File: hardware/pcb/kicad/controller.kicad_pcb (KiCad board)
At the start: 6 copper layers, 160 x 100 mm, 0 parts

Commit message: feat(hardware): complete reproducible engineering release artifacts
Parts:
- added F1: FUSE_10A, , F.Cu at (48.0, 35.0)
- added H1: M3_NPTH, , F.Cu at (24.0, 24.0)
- added H2: M3_NPTH, , F.Cu at (176.0, 24.0)
- added H3: M3_NPTH, , F.Cu at (176.0, 116.0)
- added H4: M3_NPTH, , F.Cu at (24.0, 116.0)
- added J1: 48V_INPUT_10A, , F.Cu at (30.0, 35.0)
- added J10: ESTOP_RED_KEYED, , F.Cu at (150.0, 110.0)
- added J2: 12V_OUTPUT_16A, , F.Cu at (72.0, 82.0)
- added J3: JETSON_5V_12A, , F.Cu at (148.0, 42.0)
- added J5: CAN_A, , F.Cu at (150.0, 96.0)
- added J6: CAN_B, , F.Cu at (168.0, 96.0)
- added U1: LM5069_HOTSWAP, , F.Cu at (68.0, 35.0)
- added U2: DCM3623_48V_12V_240W, , F.Cu at (88.0, 35.0)
- added U3: BUCK_12V_5V_10A, , F.Cu at (112.0, 42.0)
- added U4: BUCK_12V_3V3_5A, , F.Cu at (112.0, 64.0)
- added U5: CH32V307_CARRIER, , F.Cu at (145.0, 64.0)
- added U6: ISO1042DW, , F.Cu at (112.0, 96.0)
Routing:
- net GND: track 0.00 -> 704.0 mm
- net 12V_ISO: track 0.00 -> 220.0 mm
- net 3V3_LOGIC: track 0.00 -> 210.0 mm
- net VBAT_FUSED: track 0.00 -> 150.5 mm
- net GND_PWR: track 0.00 -> 83.5 mm
- net CANL: track 0.00 -> 70.0 mm
- net CANH: track 0.00 -> 70.0 mm
- net 5V_JETSON: track 0.00 -> 53.0 mm
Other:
- board text added: "8 mm ISOLATION BARRIER"
- board text added: "LOGIC / INTERFACES"
- board text added: "POWER DOMAIN"
- board text added: "WORKBENCH-1 CONTROLLER REV A"
- board text removed: "8 mm ISOLATION BARRIER - NO COPPER"
- board text removed: "WORKBENCH-1 CONTROLLER - NOT FOR FABRICATION"

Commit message: feat(hardware): close EVT interface and isolation review
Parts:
- added J4: JETSON_MCU_BACKPLANE, , F.Cu at (145.0, 140.0)
- added U7: 3V3_5V_ISOLATED_DC_DC, , F.Cu at (165.0, 77.0)
- J3: value JETSON_5V_12A -> JETSON_DEVKIT_12V_5A
- U3: value BUCK_12V_5V_10A -> JETSON_12V_EFUSE_5A
- moved J10 85.4 mm to (70.0, 140.0)
- moved U5 46.0 mm to (145.0, 110.0)
- moved J5 41.3 mm to (145.0, 55.0)
- moved J6 41.1 mm to (165.0, 55.0)
- moved U6 38.1 mm to (145.0, 77.0)
- moved J2 34.0 mm to (106.0, 82.0)
- moved H3 30.0 mm to (176.0, 146.0)
- moved H4 30.0 mm to (24.0, 146.0)
- moved J3 23.0 mm to (125.0, 42.0)
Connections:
- net 5V_JETSON renamed JETSON_12V
- J5 pad 3: GND -> GND_CAN_ISO
- J6 pad 3: GND -> GND_CAN_ISO
- U5 pad 2: 3V3_LOGIC -> GND
- U5 pad 4: 3V3_LOGIC -> GND
- U5 pad 5: GND -> SPI_SCLK
- U5 pad 6: GND -> SPI_MOSI
- U5 pad 7: GND -> SPI_MISO
- U5 pad 8: GND -> MOTOR_ENABLE
- U6 pad 1: 3V3_LOGIC -> 5V_CAN_ISO
- U6 pad 2: GND -> GND_CAN_ISO
- U6 pad 3: (no net) -> CANH
- U6 pad 4: (no net) -> CANL
- U6 pad 5: CANH -> 3V3_LOGIC
- U6 pad 6: CANL -> GND
- U6 pad 7: GND -> CAN_TX
- U6 pad 8: 3V3_LOGIC -> CAN_RX
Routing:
- net GND: track 704.0 -> 930.8 mm
- net 12V_ISO: track 220.0 -> 158.5 mm
- net GND_CAN_ISO: track 0.00 -> 59.0 mm
- net CAN_TX: track 0.00 -> 47.6 mm
- net CAN_RX: track 0.00 -> 47.4 mm
- net UART_TX: track 0.00 -> 30.1 mm
- net UART_RX: track 0.00 -> 30.1 mm
- net SPI_SCLK: track 0.00 -> 30.1 mm
- net SPI_MOSI: track 0.00 -> 30.1 mm
- net SPI_MISO: track 0.00 -> 30.1 mm
- net MOTOR_ENABLE: track 0.00 -> 30.1 mm
- net MOTOR_CS5: track 0.00 -> 30.1 mm
- net MOTOR_CS4: track 0.00 -> 30.1 mm
- net MOTOR_CS3: track 0.00 -> 30.1 mm
- net MOTOR_CS2: track 0.00 -> 30.1 mm
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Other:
- board size 160 x 100 mm -> 160 x 130 mm
- board text added: "CAN ISOLATION"

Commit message: feat(hardware): harden safety and order release gates
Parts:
- added J11: SAFETY_GATE_OUTPUT, , F.Cu at (135.0, 92.0)
- added U8: DUAL_CHANNEL_SAFETY_GATE_CARRIER, , F.Cu at (110.0, 125.0)
- J10: value ESTOP_RED_KEYED -> ESTOP_RED_KEYED_DUAL_CHANNEL
- moved J10 38.0 mm to (108.0, 140.0)
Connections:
- net MOTOR_ENABLE renamed MOTOR_ENABLE_REQ
- J10 pad 1: (no net) -> ESTOP_CH_A_OUT
- J10 pad 2: (no net) -> ESTOP_CH_A_RETURN
- J10 pad 3: (no net) -> ESTOP_CH_B_OUT
- J10 pad 4: (no net) -> ESTOP_CH_B_RETURN
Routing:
- net ESTOP_SENSE: track 30.1 -> 170.3 mm, vias 0 -> 2
- net GND: track 930.8 -> 1023.4 mm, vias 0 -> 3
- net MOTOR_ENABLE_REQ: track 30.1 -> 93.5 mm, vias 0 -> 1
- net MOTOR_ENABLE_SAFE: track 0.00 -> 60.0 mm
- net 12V_ISO: track 158.5 -> 204.0 mm, vias 0 -> 1
- net 3V3_LOGIC: track 190.3 -> 207.9 mm, vias 0 -> 1
- net ESTOP_CH_A_OUT: track 0.00 -> 16.0 mm
- net ESTOP_CH_A_RETURN: track 0.00 -> 15.7 mm
- net ESTOP_CH_B_OUT: track 0.00 -> 15.4 mm
- net ESTOP_CH_B_RETURN: track 0.00 -> 15.2 mm

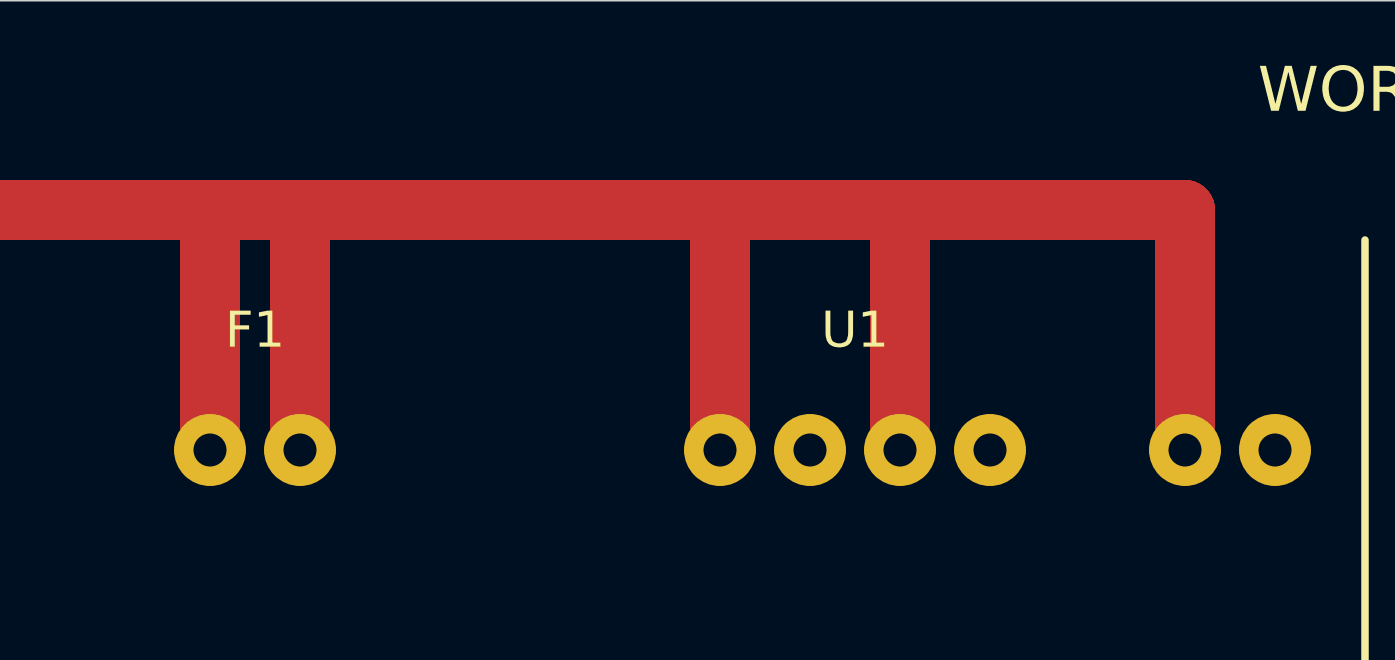
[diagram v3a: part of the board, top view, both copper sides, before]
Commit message: feat(hardware): audit protected input connectivity
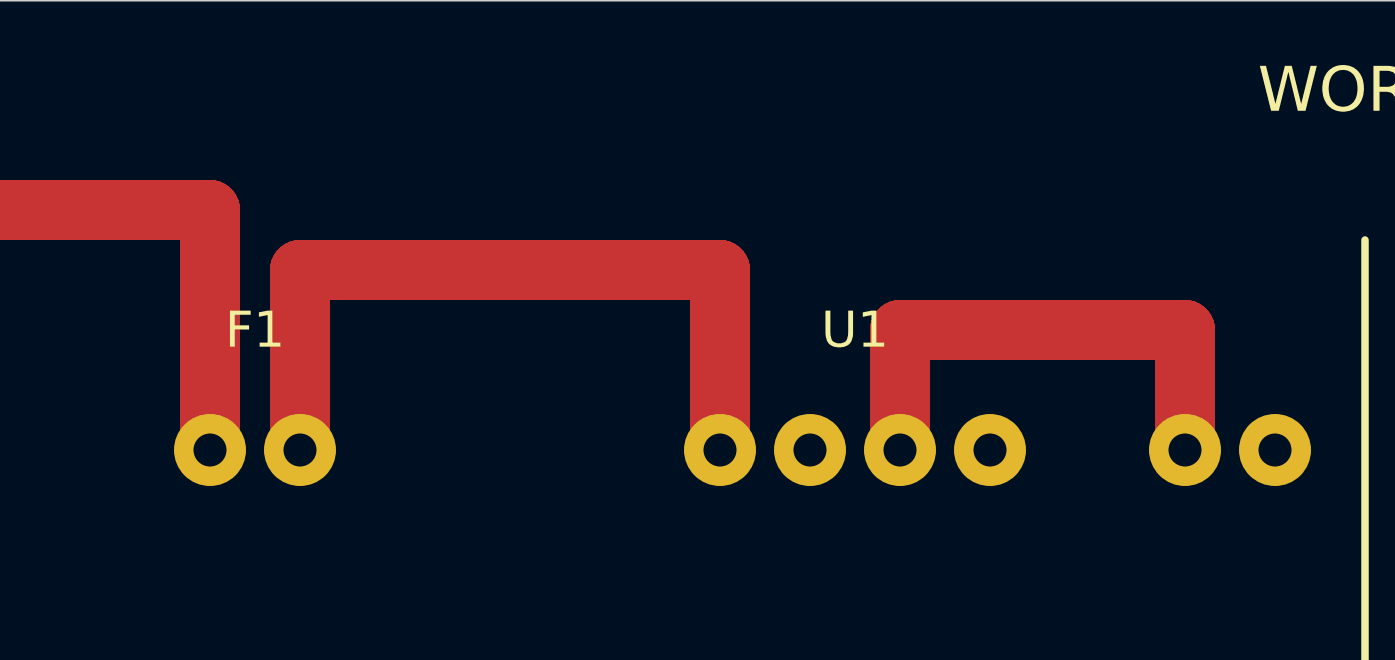
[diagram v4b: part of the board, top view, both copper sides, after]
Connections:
- F1 pad 1: VBAT_FUSED -> VBAT_RAW
- J1 pad 1: VBAT_FUSED -> VBAT_RAW
- J1 pad 2: VBAT_FUSED -> VBAT_RAW
- U1 pad 3: VBAT_FUSED -> VBAT_PROTECTED
- U2 pad 1: VBAT_FUSED -> VBAT_PROTECTED
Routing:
- net VBAT_FUSED: track 149.5 -> 26.0 mm
- net VBAT_RAW: track 0.00 -> 53.0 mm
- net VBAT_PROTECTED: track 0.00 -> 17.5 mm

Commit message: feat(hardware): add measured testpoint coverage
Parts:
- added TP1: VBAT_PROTECTED, , F.Cu at (69.5, 42.0)
- added TP2: 12V_ISO, , F.Cu at (101.5, 88.0)
- added TP3: JETSON_12V, , F.Cu at (120.5, 48.0)
- added TP4: 3V3_LOGIC, , F.Cu at (113.5, 70.0)
- added TP5: GND, , F.Cu at (116.5, 70.0)
- added TP6: CANH, , F.Cu at (140.5, 48.0)
- added TP7: CANL, , F.Cu at (143.5, 48.0)
- added TP8: MCU_RESET, , F.Cu at (168.4, 103.0)
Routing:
- net VBAT_PROTECTED: track 17.5 -> 24.5 mm
- net MCU_RESET: track 30.1 -> 37.1 mm
- net CANL: track 44.0 -> 51.0 mm
- net CANH: track 44.0 -> 51.0 mm
- net JETSON_12V: track 30.0 -> 36.0 mm
- net GND: track 1023.4 -> 1029.4 mm
- net 3V3_LOGIC: track 207.9 -> 213.9 mm
- net 12V_ISO: track 204.0 -> 210.0 mm

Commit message: feat(hardware): complete service robot engineering baseline
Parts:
- added C1: 1uF 100V, C_1210_3225Metric, F.Cu at (31.0, 36.0)
- added C10: 100nF, C_0603_1608Metric, F.Cu at (95.5, 102.5)
- added C11: 100nF, C_0603_1608Metric, F.Cu at (95.5, 105.7)
- added C12: 100nF, C_0603_1608Metric, F.Cu at (95.5, 108.9)
- added C13: 100nF, C_0603_1608Metric, F.Cu at (100.8, 113.0)
- added C14: 100nF, C_0603_1608Metric, F.Cu at (111.8, 113.0)
- added C15: 100nF, C_0603_1608Metric, F.Cu at (116.0, 97.2)
- added C16: 100nF, C_0603_1608Metric, F.Cu at (100.2, 93.0)
- added C17: 4.7uF, C_0805_2012Metric, F.Cu at (108.0, 91.5)
- added C18: 100nF, C_0603_1608Metric, F.Cu at (112.0, 18.0)
- added C19: 100nF, C_0603_1608Metric, F.Cu at (122.0, 111.0)
- added C2: 10uF 100V, C_2220_5750Metric, F.Cu at (42.0, 31.5)
- added C20: 1uF 10V, C_0603_1608Metric, F.Cu at (110.0, 46.8)
- added C3: 470uF 25V, CP_Radial_D12.5mm_P5.00mm, F.Cu at (93.0, 27.0)
- added C4: 1uF 25V, C_0805_2012Metric, F.Cu at (110.5, 6.50)
- added C40: 100nF, C_0603_1608Metric, F.Cu at (127.8, 36.2)
- added C41: 100nF, C_0603_1608Metric, F.Cu at (142.2, 36.2)
- added C42: 4.7uF, C_0805_2012Metric, F.Cu at (133.2, 18.0)
- added C43: 4.7uF, C_0805_2012Metric, F.Cu at (144.7, 18.0)
- added C44: 100nF, C_0603_1608Metric, F.Cu at (142.2, 42.5)
- added C5: 220uF 25V, CP_Radial_D10.0mm_P5.00mm, F.Cu at (119.0, 20.5)
- added C6: 22uF 25V, C_1210_3225Metric, F.Cu at (92.0, 43.5)
- added C7: 47uF 10V, C_1210_3225Metric, F.Cu at (87.5, 56.5)
- added C8: 47uF 10V, C_1210_3225Metric, F.Cu at (93.0, 56.5)
- added C9: 100nF, C_0603_1608Metric, F.Cu at (95.5, 99.3)
- added CG1: 4.7nF 100V, C_0603_1608Metric, F.Cu at (25.5, 26.5)
- added CSS4: 22nF, C_0603_1608Metric, F.Cu at (106.0, 46.8)
- added CY1: 18pF, C_0603_1608Metric, F.Cu at (88.5, 102.5)
- added CY2: 18pF, C_0603_1608Metric, F.Cu at (92.0, 106.5)
- added D1: SMCJ58A, D_SMC, F.Cu at (32.0, 10.5)
- added D2: CAN FD TVS, CAN_TVS, F.Cu at (150.0, 53.0)
- added D3: FLYBACK, D_SOD-123, F.Cu at (20.0, 82.5)
- added D4: FLYBACK, D_SOD-123, F.Cu at (20.0, 103.5)
- added F2: PTC 0.25A, Fuse_1206_3216Metric, F.Cu at (62.3, 86.2)
- added J12: DUAL MANUAL RESET, MicroFit_2x2, F.Cu at (71.0, 107.0)
- added J13: WCH DEBUG, PinHeader_1x04_P2.54mm_Vertical, F.Cu at (134.0, 115.5)
- added JP1: CAN TERM, PinHeader_1x02_P2.54mm_Vertical, F.Cu at (148.0, 84.0)
- added K1: FORCE-GUIDED 12V A, Panasonic_SFM4, F.Cu at (29.0, 93.0)
- added K2: FORCE-GUIDED 12V B, Panasonic_SFM4, F.Cu at (29.0, 114.0)
- added L1: 100R@100MHz, ACT45B, F.Cu at (144.0, 48.0)
- added Q1: 150V N-MOS, Infineon_PG-TDSON-8_6.15x5.15mm, F.Cu at (22.0, 21.0)
- added Q2: 150V N-MOS, Infineon_PG-TDSON-8_6.15x5.15mm, F.Cu at (30.0, 21.0)
- added R30: 33R, R_0603_1608Metric, F.Cu at (100.0, 118.0)
- added R31: 33R, R_0603_1608Metric, F.Cu at (104.0, 118.0)
- added R32: 33R, R_0603_1608Metric, F.Cu at (108.0, 118.0)
- added R33: 33R, R_0603_1608Metric, F.Cu at (112.0, 118.0)
- added R34: 33R, R_0603_1608Metric, F.Cu at (116.0, 118.0)
- added R35: 33R, R_0603_1608Metric, F.Cu at (120.0, 118.0)
- added R36: 33R, R_0603_1608Metric, F.Cu at (124.0, 118.0)
- added R37: 33R, R_0603_1608Metric, F.Cu at (100.0, 123.0)
- added R38: 33R, R_0603_1608Metric, F.Cu at (104.0, 123.0)
- added R39: 33R, R_0603_1608Metric, F.Cu at (108.0, 123.0)
- added R40: 33R, R_0603_1608Metric, F.Cu at (112.0, 123.0)
- added R41: 33R, R_0603_1608Metric, F.Cu at (116.0, 123.0)
- added R42: 33R, R_0603_1608Metric, F.Cu at (120.0, 123.0)
- added R43: 100k, R_0603_1608Metric, F.Cu at (118.0, 115.0)
- added R44: 100k, R_0603_1608Metric, F.Cu at (61.5, 91.8)
- added R45: 100k, R_0603_1608Metric, F.Cu at (61.5, 94.3)
- added R46: 100k, R_0603_1608Metric, F.Cu at (102.0, 46.8)
- added R47: 10k, R_0603_1608Metric, F.Cu at (91.5, 6.75)
- added R48: 3.00k 1%, R_0603_1608Metric, F.Cu at (108.0, 18.0)
- added R49: 10k, R_0603_1608Metric, F.Cu at (52.5, 98.3)
- added R50: 10k, R_0603_1608Metric, F.Cu at (56.5, 98.3)
- added R51: 10k, R_0603_1608Metric, F.Cu at (115.0, 6.75)
- added R52: 4.7k, R_0603_1608Metric, F.Cu at (61.5, 96.8)
- added R53: 4.7k, R_0603_1608Metric, F.Cu at (48.5, 98.3)
- added R54: 10k, R_0603_1608Metric, F.Cu at (118.0, 111.0)
- added R55: 4.7k, R_0603_1608Metric, F.Cu at (124.0, 114.0)
- added R56: 4.7k, R_0603_1608Metric, F.Cu at (128.0, 114.0)
- added R57: 100k, R_0603_1608Metric, F.Cu at (61.5, 89.3)
- added R58: 120R 1%, R_1206_3216Metric, F.Cu at (143.0, 84.0)
- added R59: 73.2k 1%, R_0603_1608Metric, F.Cu at (108.0, 26.0)
- added R60: 10.0k 1%, R_0603_1608Metric, F.Cu at (112.0, 26.0)
- added RFB1: 45.0k 1%, R_0603_1608Metric, F.Cu at (94.0, 46.8)
- added RFB2: 10.0k 1%, R_0603_1608Metric, F.Cu at (98.0, 46.8)
- added RG1: 22k, R_0603_1608Metric, F.Cu at (22.0, 26.5)
- added RPG1: 453k 1%, R_0603_1608Metric, F.Cu at (108.0, 22.0)
- added RPG2: 56.0k 1%, R_0603_1608Metric, F.Cu at (112.0, 22.0)
- added RPG3: 10k, R_0603_1608Metric, F.Cu at (87.5, 6.75)
- added RS1: 6mR 3W 1%, Sense_3637, F.Cu at (39.5, 21.0)
- added RSH1: 510k, R_0603_1608Metric, F.Cu at (36.0, 34.0)
- added RUV1: 19.6M 1%, R_1206_3216Metric, F.Cu at (10.0, 26.5)
- added RUV2: 133k 1%, R_0603_1608Metric, F.Cu at (14.0, 26.5)
- added RUV3: 162k 1%, R_0603_1608Metric, F.Cu at (18.0, 30.5)
- added Y1: 8MHz, Crystal_SMD_3225-4Pin_3.2x2.5mm, F.Cu at (92.0, 103.0)
- F1: value FUSE_10A -> 10A 125V; footprint (none) -> Fuse_4510
- J1: value 48V_INPUT_10A -> 48V INPUT; footprint (none) -> MicroFit_2x2
- J10: value ESTOP_RED_KEYED_DUAL_CHANNEL -> DUAL ESTOP LOOP; footprint (none) -> MicroFit_2x2
- J11: value SAFETY_GATE_OUTPUT -> SAFETY OUTPUT; footprint (none) -> MicroFit_2x2
- J2: value 12V_OUTPUT_16A -> 12V MOTOR AUX; footprint (none) -> MicroFit_2x2
- J3: value JETSON_DEVKIT_12V_5A -> JETSON DEVKIT 12V; footprint (none) -> MicroFit_2x2
- J4: value JETSON_MCU_BACKPLANE -> JETSON MCU BACKPLANE; footprint (none) -> PinHeader_2x10_P2.54mm_Vertical
- J5: value CAN_A -> CAN A; footprint (none) -> MicroFit_2x2
- J6: value CAN_B -> CAN B; footprint (none) -> MicroFit_2x2
- TP1, TP2, TP3, TP4, TP5, TP6, TP7, TP8: footprint (none) -> TestPoint_Pad_D1.5mm
- U1: value LM5069_HOTSWAP -> LTC4368HMS-2; footprint (none) -> MSOP-10_3x3mm_P0.5mm
- U2: value DCM3623_48V_12V_240W -> ISOLATED 48V-12V 240W (TBD); footprint (none) -> Isolated_48V_12V_240W_TBD
- U3: value JETSON_12V_EFUSE_5A -> TPS26633RGE; footprint (none) -> TPS26633_RGE24
- U4: value BUCK_12V_3V3_5A -> RPL-5.0 3V3/5A; footprint (none) -> RPL-5.0_QFN24
- U5: value CH32V307_CARRIER -> CH32V307VCT6; footprint (none) -> LQFP-100_14x14mm_P0.5mm
- U6: footprint (none) -> ISO1042_DW16_HV
- U7: value 3V3_5V_ISOLATED_DC_DC -> 3V3-5V ISO 1W; footprint (none) -> Converter_DCDC_muRata_MEJ1SxxxxSC_THT
- U8: value DUAL_CHANNEL_SAFETY_GATE_CARRIER -> ESTOP DIAGNOSTIC OPTO; footprint (none) -> SOIC-16W_7.5x10.3mm_P1.27mm
- moved J11 83.4 mm to (53.0, 107.0)
- moved J4 76.3 mm to (82.0, 97.0)
- moved TP1 73.4 mm to (8.00, 82.0)
- moved TP8 67.7 mm to (104.0, 82.0)
- moved U8 66.4 mm to (53.0, 91.0)
- moved U7 62.4 mm to (132.0, 24.0)
- moved J10 61.4 mm to (71.0, 91.0)
- moved TP3 59.2 mm to (72.0, 82.0)
- moved TP7 40.9 mm to (152.0, 88.0)
- moved TP6 40.0 mm to (141.0, 88.0)
- moved TP2 40.0 mm to (62.0, 82.0)
- moved U5 39.6 mm to (106.0, 103.0)
- moved J3 38.6 mm to (102.4, 10.8)
- moved U6 38.3 mm to (135.0, 40.0)
- moved U1 34.3 mm to (34.5, 27.7)
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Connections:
- J10 pad 1: ESTOP_CH_A_OUT -> ESTOP_12V
- J10 pad 3: ESTOP_CH_B_OUT -> ESTOP_12V
- J11 pad 4: (no net) -> 3V3_LOGIC
- J4 pad 8: MOTOR_ENABLE_REQ -> JETSON_ENABLE_REQ
- U1 pad 1: VBAT_FUSED -> GND_PWR
- U1 pad 3: VBAT_PROTECTED -> OV_SET
- U1 pad 4: GND_PWR -> UV_SET
- U2 pad 3: 12V_ISO -> (no net)
- U2 pad 4: GND -> 12V_ISO
- U3 pad 2: GND -> 12V_ISO
- U3 pad 3: JETSON_12V -> (no net)
- U3 pad 4: GND -> (no net)
- U4 pad 1: 12V_ISO -> GND
- U4 pad 3: 3V3_LOGIC -> GND
- U5 pad 1: 3V3_LOGIC -> (no net)
- U5 pad 10: MOTOR_CS1 -> GND
- U5 pad 11: MOTOR_CS2 -> 3V3_LOGIC
- U5 pad 12: MOTOR_CS3 -> OSC_IN
- U5 pad 13: MOTOR_CS4 -> OSC_OUT
- U5 pad 14: MOTOR_CS5 -> MCU_RESET
- U5 pad 15: I2C_SDA -> (no net)
- U5 pad 16: I2C_SCL -> (no net)
- U5 pad 17: ESTOP_SENSE -> (no net)
- U5 pad 18: UART_TX -> (no net)
- U5 pad 19: UART_RX -> GND
- U5 pad 2: GND -> (no net)
- U5 pad 20: MCU_RESET -> GND
- U5 pad 21: CAN_TX -> 3V3_LOGIC
- U5 pad 22: CAN_RX -> 3V3_LOGIC
- U5 pad 3: 3V3_LOGIC -> (no net)
- U5 pad 4: GND -> (no net)
- U5 pad 5: SPI_SCLK -> (no net)
- U5 pad 6: SPI_MOSI -> 3V3_LOGIC
- U5 pad 7: SPI_MISO -> (no net)
- U5 pad 8: MOTOR_ENABLE_REQ -> (no net)
- U5 pad 9: MOTOR_CS0 -> (no net)
- U6 pad 1: 5V_CAN_ISO -> 3V3_LOGIC
- U6 pad 2: GND_CAN_ISO -> GND
- U6 pad 3: CANH -> CAN_TX
- U6 pad 4: CANL -> (no net)
- U6 pad 5: 3V3_LOGIC -> CAN_RX
- U6 pad 6: GND -> (no net)
- U6 pad 7: CAN_TX -> (no net)
- U6 pad 8: CAN_RX -> GND
- U7 pad 1: 5V_CAN_ISO -> 3V3_LOGIC
- U7 pad 2: GND_CAN_ISO -> GND
- U7 pad 5: 3V3_LOGIC -> GND_CAN_ISO
- U7 pad 7: (no net) -> 5V_CAN_ISO
- U8 pad 1: 12V_ISO -> ESTOP_CH_A_RETURN
- U8 pad 10: GND -> (no net)
- U8 pad 11: 3V3_LOGIC -> (no net)
- U8 pad 2: GND -> U8_LED_A_K
- U8 pad 3: MOTOR_ENABLE_REQ -> ESTOP_CH_B_RETURN
- U8 pad 4: MOTOR_ENABLE_SAFE -> U8_LED_B_K
- U8 pad 5: ESTOP_SENSE -> (no net)
- U8 pad 6: ESTOP_CH_A_OUT -> (no net)
- U8 pad 7: ESTOP_CH_A_RETURN -> (no net)
- U8 pad 8: ESTOP_CH_B_OUT -> (no net)
- U8 pad 9: ESTOP_CH_B_RETURN -> (no net)
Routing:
- net GND: track 1029.4 -> 582.5 mm, vias 3 -> 38
- net 3V3_LOGIC: track 213.9 -> 487.8 mm, vias 1 -> 9
- net RELAY_B_NC: track 0.00 -> 113.5 mm, vias 0 -> 2
- net RELAY_A_NC: track 0.00 -> 107.3 mm, vias 0 -> 2
- net JETSON_12V: track 36.0 -> 141.9 mm, vias 0 -> 6
- net ESTOP_A_MON: track 0.00 -> 78.0 mm, vias 0 -> 3
- net VBAT_PROTECTED: track 24.5 -> 100.1 mm, vias 0 -> 5
- net ESTOP_B_MON: track 0.00 -> 72.2 mm, vias 0 -> 3
- net RESET_CH_B_RETURN: track 0.00 -> 70.3 mm
- net RESET_CH_A_RETURN: track 0.00 -> 68.2 mm
- net ESTOP_CH_B_RETURN: track 15.2 -> 79.1 mm, vias 0 -> 1
- net ESTOP_CH_A_RETURN: track 15.7 -> 74.1 mm
- net ESTOP_SENSE: track 170.3 -> 113.0 mm
- net VBAT_RAW: track 53.0 -> 9.88 mm, vias 0 -> 1
- net MOTOR_ENABLE_SAFE: track 60.0 -> 17.5 mm
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- added copper zone on In2.Cu, net 12V_ISO
- added copper zone on F.Cu, net 3V3_LOGIC
- added copper zone on In5.Cu, net 3V3_LOGIC
- added copper zone on In5.Cu, net 5V_CAN_ISO
- added copper zone on F.Cu, net FET_COMMON
- added copper zone on In1.Cu, net GND
- added copper zone on In4.Cu, net GND
- added copper zone on B.Cu, net GND_CAN_ISO
- added copper zone on F.Cu, net GND_CAN_ISO
- added copper zone on In1.Cu, net GND_CAN_ISO
- added copper zone on In4.Cu, net GND_CAN_ISO
- added copper zone on B.Cu, net GND_PWR
- added copper zone on F.Cu, net GND_PWR
- added copper zone on In1.Cu, net GND_PWR
- added copper zone on F.Cu, net INPUT_SENSE
- added copper zone on B.Cu, net JETSON_12V
- added copper zone on F.Cu, net JETSON_12V
- added copper zone on In3.Cu, net JETSON_12V
- added copper zone on F.Cu, net VBAT_FUSED
- added copper zone on F.Cu, net VBAT_PROTECTED
- added copper zone on F.Cu, net VBAT_RAW
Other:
- copper layers 6 -> 8
- board text added: "12V / LOGIC SECONDARY"
- board text added: "48V PRIMARY"
- board text added: "DO NOT FIT"
- board text added: "DO NOT ORDER WITHOUT RELEASE APPROVAL"
- board text added: "FAB: ENIG | THK 1.60 +/- 0.16 MM (MASK EXCL)"
- board text added: "FAB: U3 HDI 9x 0.45/0.15 FILL/CAP/PLANARIZE"
- board text added: "ISOLATED CAN FD"
- board text added: "PRIMARY | SECONDARY"
- board text added: "U2 LAND PATTERN TBD"
- board text added: "WORKBENCH-1 CONTROLLER EVT1"
- board text removed: "8 mm ISOLATION BARRIER"
- board text removed: "CAN ISOLATION"
- board text removed: "LOGIC / INTERFACES"
- board text removed: "POWER DOMAIN"
- board text removed: "WORKBENCH-1 CONTROLLER REV A"
